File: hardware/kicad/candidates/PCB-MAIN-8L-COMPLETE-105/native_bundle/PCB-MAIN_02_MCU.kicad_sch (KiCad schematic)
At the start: 27 parts, among them U1 STM32U585VIT6Q, X1 32.768 kHz full-swing LVCMOS

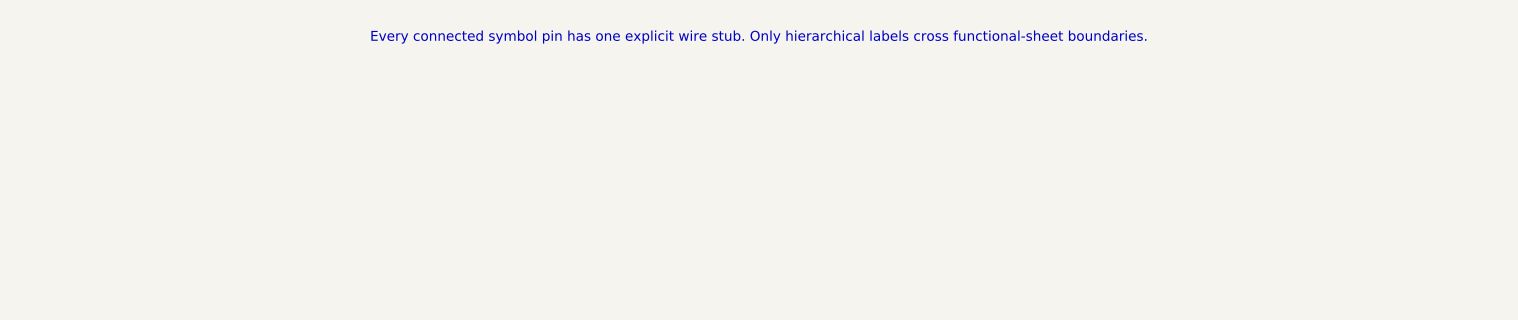
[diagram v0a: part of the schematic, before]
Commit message: PCB-MAIN Rev B: bilingual schematic notes and PDF
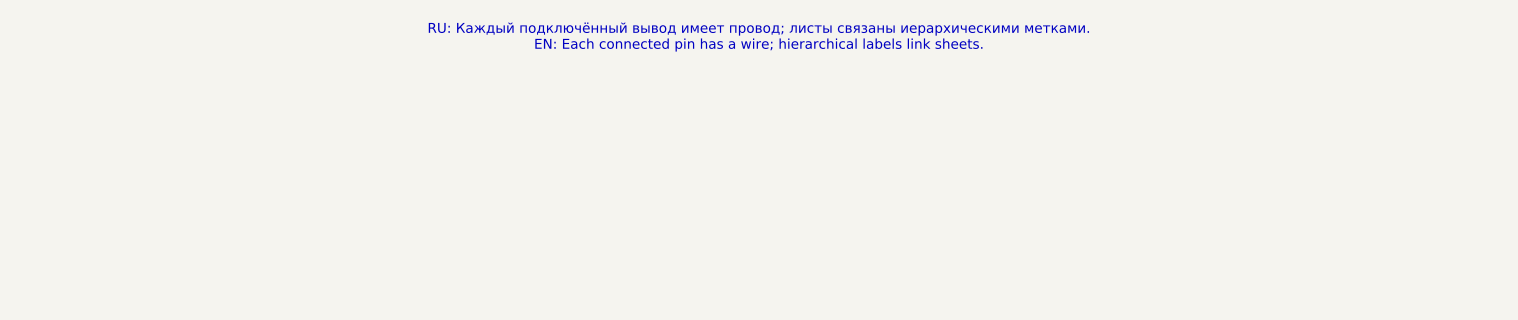
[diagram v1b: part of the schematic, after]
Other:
- note added: "RU: Каждый подключённый вывод имеет провод; листы связаны иерархическими метками. EN: Each connected pin has a wire; hierarchical labels link sheets."
- note removed: "Every connected symbol pin has one explicit wire stub. Only hierarchical labels cross functional-sheet boundaries."
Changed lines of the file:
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@@
     (stroke (width 0.0))
   )
-  (text "Every connected symbol pin has one explicit wire stub. Only hierarchical labels cross functional-sheet boundaries."
+  (text "RU: Каждый подключённый вывод имеет провод; листы связаны иерархическими метками.\nEN: Each connected pin has a wire; hierarchical labels link sheets."
     (at 297.0 12.7 0)
     (effects (font (size 1.1 1.1)))
